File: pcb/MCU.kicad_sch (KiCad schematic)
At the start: 14 parts, among them U1 WeMos_S2_mini

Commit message: added connector and simulation link
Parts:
- removed TP28, TP29, TP30: TestPoint, Connector_PinHeader_1.00mm:PinHeader_1x01_P1.00mm_Vertical, symbol Connector:TestPoint
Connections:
- net SCR_QS_KS: now reaches U1.20 (GPIO6)
- net T_RPM: now reaches U1.19 (GPIO4)
- net T_CUT: now reaches U1.3 (GPIO5)
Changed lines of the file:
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@@
+		)
+	)
+	(global_label "SCR_QS_KS"
+		(shape input)
+		(at 86.36 64.77 0)
+		(fields_autoplaced yes)
+		(effects
+			(font
+				(size 1.27 1.27)
+			)
+			(justify left)
+		)
+		(property "Intersheetrefs" "${INTERSHEET_REFS}"
+			(at 100.0494 64.77 0)
+			(effects
+				(font
+					(size 1.27 1.27)
+				)
+				(justify left)
+				(hide yes)
+			)
 		)
 	)
@@
 		)
 	)
+	(global_label "T_RPM"
+		(shape input)
+		(at 86.36 59.69 0)
+		(fields_autoplaced yes)
+		(effects
+			(font
+				(size 1.27 1.27)
+			)
+			(justify left)
+		)
+		(property "Intersheetrefs" "${INTERSHEET_REFS}"
+			(at 95.2718 59.69 0)
+			(effects
+				(font
+					(size 1.27 1.27)
+				)
+				(justify left)
+				(hide yes)
+			)
+		)
+	)
+	(global_label "T_CUT"
+		(shape input)
+		(at 86.36 62.23 0)
+		(fields_autoplaced yes)
+		(effects
+			(font
+				(size 1.27 1.27)
+			)
+			(justify left)
+		)
+		(property "Intersheetrefs" "${INTERSHEET_REFS}"
+			(at 94.8485 62.23 0)
+			(effects
+				(font
+					(size 1.27 1.27)
+				)
+				(justify left)
+				(hide yes)
+			)
+		)
+	)
 	(global_label "PWM_VR"
 		(shape input)
@@
 	)
 	(symbol
-		(lib_id "Connector:TestPoint")
-		(at 86.36 64.77 270)
-		(unit 1)
-		(exclude_from_sim no)
-		(in_bom yes)
-		(on_board yes)
-		(dnp no)
-		(property "Reference" "TP28"
-			(at 91.186 64.77 90)
-			(effects
-				(font
-					(size 1.27 1.27)
-				)
-				(justify left)
-			)
-		)
-		(property "Value" "TestPoint"
-			(at 88.3921 67.31 0)
-			(effects
-				(font
-					(size 1.27 1.27)
-				)
-				(justify left)
-				(hide yes)
-			)
-		)
-		(property "Footprint" "Connector_PinHeader_1.00mm:PinHeader_1x01_P1.00mm_Vertical"
-			(at 86.36 69.85 0)
-			(effects
-				(font
-					(size 1.27 1.27)
-				)
-				(hide yes)
-			)
-		)
-		(property "Datasheet" "~"
-			(at 86.36 69.85 0)
-			(effects
-				(font
-					(size 1.27 1.27)
-				)
-				(hide yes)
-			)
-		)
-		(property "Description" "test point"
-			(at 86.36 64.77 0)
-			(effects
-				(font
-					(size 1.27 1.27)
-				)
-				(hide yes)
-			)
-		)
-		(pin "1"
-		)
-		(instances
-			(project "ecu-dev-board"
-				(path "/38d4df77-b5a0-4642-8410-8b13c21c2c3b/5baacb37-d82a-49c1-a6be-f8a839583d33"
-					(reference "TP28")
-					(unit 1)
-				)
-			)
-		)
-	)
-	(symbol
 		(lib_id "power:GND")
 		(at 265.43 52.07 0)
@@
 	)
 	(symbol
-		(lib_id "Connector:TestPoint")
-		(at 86.36 59.69 270)
-		(unit 1)
-		(exclude_from_sim no)
-		(in_bom yes)
-		(on_board yes)
-		(dnp no)
-		(property "Reference" "TP30"
-			(at 90.932 59.69 90)
-			(effects
-				(font
-					(size 1.27 1.27)
-				)
-				(justify left)
-			)
-		)
-		(property "Value" "TestPoint"
-			(at 88.3921 62.23 0)
-			(effects
-				(font
-					(size 1.27 1.27)
-				)
-				(justify left)
-				(hide yes)
-			)
-		)
-		(property "Footprint" "Connector_PinHeader_1.00mm:PinHeader_1x01_P1.00mm_Vertical"
-			(at 86.36 64.77 0)
-			(effects
-				(font
-					(size 1.27 1.27)
-				)
-				(hide yes)
-			)
-		)
-		(property "Datasheet" "~"
-			(at 86.36 64.77 0)
-			(effects
-				(font
-					(size 1.27 1.27)
-				)
-				(hide yes)
-			)
-		)
-		(property "Description" "test point"
-			(at 86.36 59.69 0)
-			(effects
-				(font
-					(size 1.27 1.27)
-				)
-				(hide yes)
-			)
-		)
-		(pin "1"
-		)
-		(instances
-			(project "ecu-dev-board"
-				(path "/38d4df77-b5a0-4642-8410-8b13c21c2c3b/5baacb37-d82a-49c1-a6be-f8a839583d33"
-					(reference "TP30")
-					(unit 1)
-				)
-			)
-		)
-	)
-	(symbol
 		(lib_id "power:GND")
 		(at 68.58 101.6 0)
@@
 					(unit 1)
 				)
-			)
-		)
-	)
-	(symbol
-		(lib_id "Connector:TestPoint")
-		(at 86.36 62.23 270)
-		(unit 1)
-		(exclude_from_sim no)
-		(in_bom yes)
-		(on_board yes)
-		(dnp no)
-		(property "Reference" "TP29"
-			(at 90.932 62.23 90)
-			(effects
-				(font
-					(size 1.27 1.27)
-				)
-				(justify left)
-			)
-		)
-		(property "Value" "TestPoint"
-			(at 88.3921 64.77 0)
-			(effects
-				(font
-					(size 1.27 1.27)
-				)
-				(justify left)
-				(hide yes)
-			)
-		)
-		(property "Footprint" "Connector_PinHeader_1.00mm:PinHeader_1x01_P1.00mm_Vertical"
-			(at 86.36 67.31 0)
-			(effects
-				(font
-					(size 1.27 1.27)
-				)
-				(hide yes)
-			)
-		)
-		(property "Datasheet" "~"
-			(at 86.36 67.31 0)
-			(effects
-				(font
-					(size 1.27 1.27)
-				)
-				(hide yes)
-			)
-		)
-		(property "Description" "test point"
-			(at 86.36 62.23 0)
-			(effects
-				(font
-					(size 1.27 1.27)
-				)
-				(hide yes)
-			)
-		)
-		(pin "1"
-		)
-		(instances
-			(project "ecu-dev-board"
-				(path "/38d4df77-b5a0-4642-8410-8b13c21c2c3b/5baacb37-d82a-49c1-a6be-f8a839583d33"
-					(reference "TP29")
-					(unit 1)
-				)

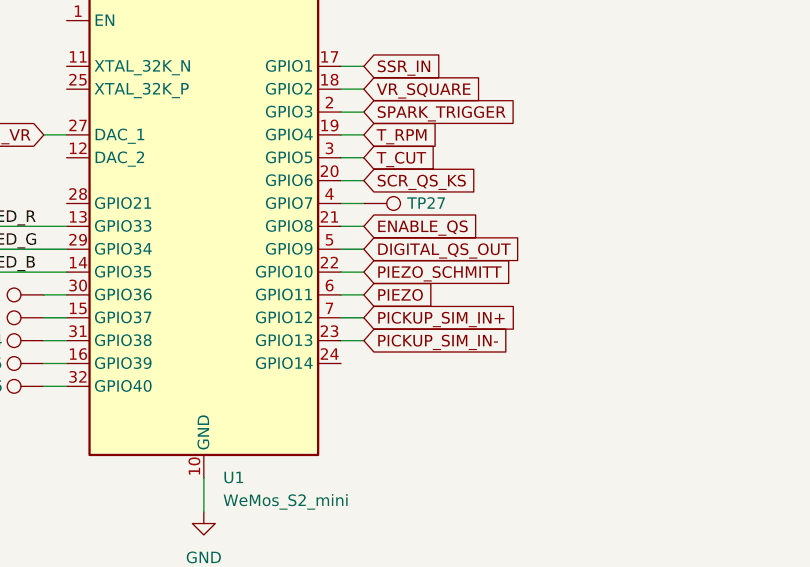
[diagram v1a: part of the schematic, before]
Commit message: added more connector tags
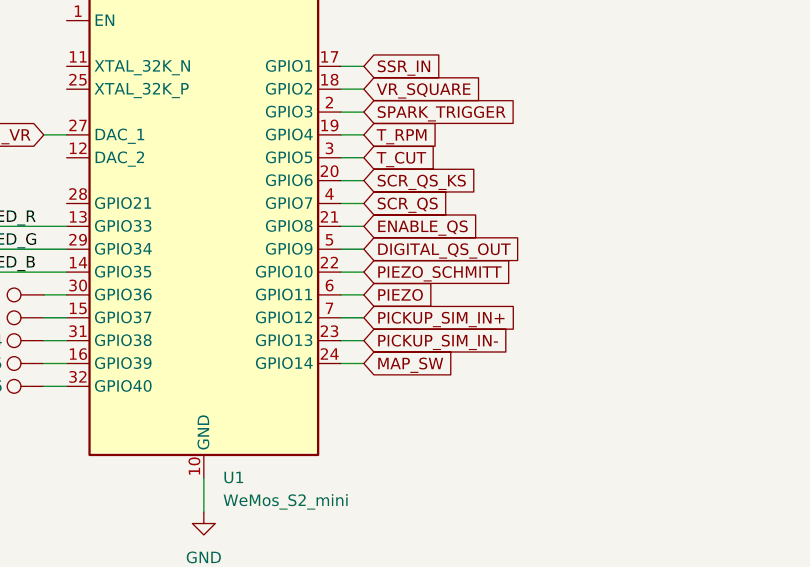
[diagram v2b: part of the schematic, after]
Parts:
- removed TP27: TestPoint, Connector_PinHeader_1.00mm:PinHeader_1x01_P1.00mm_Vertical, symbol Connector:TestPoint
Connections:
- net SCR_QS: now reaches U1.4 (GPIO7)
- net MAP_SW: now reaches U1.24 (GPIO14)
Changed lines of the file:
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@@
+	(wire
+		(pts
+			(xy 86.36 85.09) (xy 83.82 85.09)
+		)
+		(stroke
+			(width 0)
+			(type default)
+		)
+	)
 	(wire
 		(pts
@@
 		)
 	)
+	(global_label "MAP_SW"
+		(shape input)
+		(at 86.36 85.09 0)
+		(fields_autoplaced yes)
+		(effects
+			(font
+				(size 1.27 1.27)
+			)
+			(justify left)
+		)
+		(property "Intersheetrefs" "${INTERSHEET_REFS}"
+			(at 96.7837 85.09 0)
+			(effects
+				(font
+					(size 1.27 1.27)
+				)
+				(justify left)
+				(hide yes)
+			)
+		)
+	)
 	(global_label "SCR_QS_KS"
 		(shape input)
@@
 		(property "Intersheetrefs" "${INTERSHEET_REFS}"
 			(at 103.678 74.93 0)
+			(effects
+				(font
+					(size 1.27 1.27)
+				)
+				(justify left)
+				(hide yes)
+			)
+		)
+	)
+	(global_label "SCR_QS"
+		(shape input)
+		(at 86.36 67.31 0)
+		(fields_autoplaced yes)
+		(effects
+			(font
+				(size 1.27 1.27)
+			)
+			(justify left)
+		)
+		(property "Intersheetrefs" "${INTERSHEET_REFS}"
+			(at 96.6023 67.31 0)
 			(effects
 				(font
@@
 					(unit 1)
 				)
-			)
-		)
-	)
-	(symbol
-		(lib_id "Connector:TestPoint")
-		(at 86.36 67.31 270)
-		(unit 1)
-		(exclude_from_sim no)
-		(in_bom yes)
-		(on_board yes)
-		(dnp no)
-		(property "Reference" "TP27"
-			(at 91.186 67.31 90)
-			(effects
-				(font
-					(size 1.27 1.27)
-				)
-				(justify left)
-			)
-		)
-		(property "Value" "TestPoint"
-			(at 88.3921 69.85 0)
-			(effects
-				(font
-					(size 1.27 1.27)
-				)
-				(justify left)
-				(hide yes)
-			)
-		)
-		(property "Footprint" "Connector_PinHeader_1.00mm:PinHeader_1x01_P1.00mm_Vertical"
-			(at 86.36 72.39 0)
-			(effects
-				(font
-					(size 1.27 1.27)
-				)
-				(hide yes)
-			)
-		)
-		(property "Datasheet" "~"
-			(at 86.36 72.39 0)
-			(effects
-				(font
-					(size 1.27 1.27)
-				)
-				(hide yes)
-			)
-		)
-		(property "Description" "test point"
-			(at 86.36 67.31 0)
-			(effects
-				(font
-					(size 1.27 1.27)
-				)
-				(hide yes)
-			)
-		)
-		(pin "1"
-		)
-		(instances
-			(project "ecu-dev-board"
-				(path "/38d4df77-b5a0-4642-8410-8b13c21c2c3b/5baacb37-d82a-49c1-a6be-f8a839583d33"
-					(reference "TP27")
-					(unit 1)
-				)

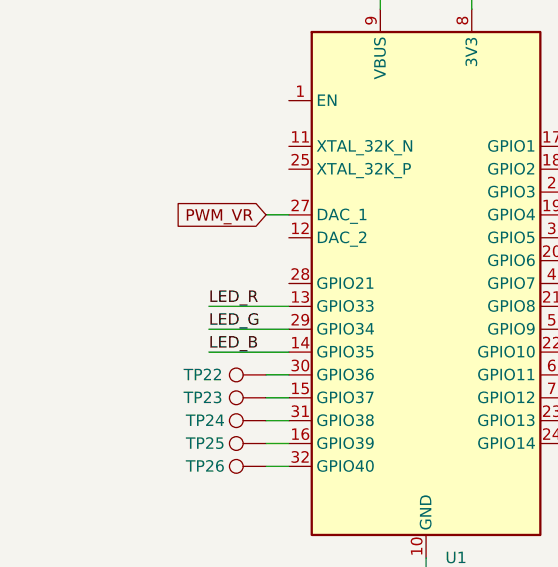
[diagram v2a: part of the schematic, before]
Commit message: enhanced pickup simulation
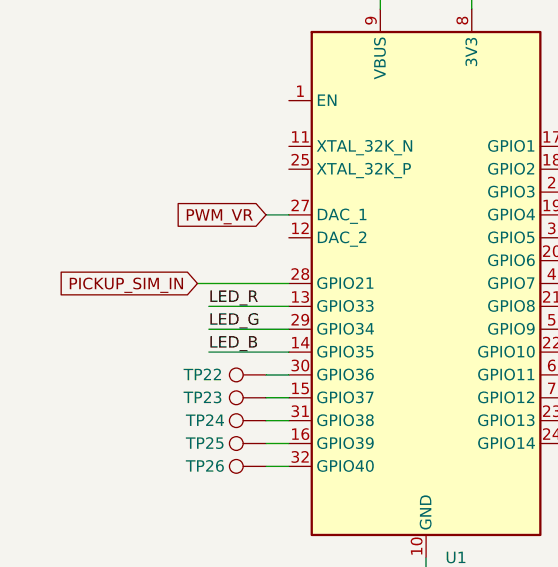
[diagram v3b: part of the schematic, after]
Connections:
- net PICKUP_SIM_IN: now reaches U1.28 (GPIO21)
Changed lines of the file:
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@@
+	(wire
+		(pts
+			(xy 43.18 67.31) (xy 53.34 67.31)
+		)
+		(stroke
+			(width 0)
+			(type default)
+		)
+	)
 	(wire
 		(pts
@@
 				(hide yes)
 			)
+		)
+	)
+	(global_label "PICKUP_SIM_IN"
+		(shape input)
+		(at 43.18 67.31 180)
+		(fields_autoplaced yes)
+		(effects
+			(font
+				(size 1.27 1.27)
+			)
+			(justify right)
+		)
+		(property "Intersheetrefs" "${INTERSHEET_REFS}"
+			(at 26.0433 67.31 0)
+			(effects
+				(font
+					(size 1.27 1.27)
+				)
+				(justify right)
+				(hide yes)
+			)

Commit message: changed capacitors and resistors footprints from 0201 to 0603
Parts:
- R50, R51, R52: footprint Resistor_SMD:R_0201_0603Metric -> Resistor_SMD:R_0603_1608Metric
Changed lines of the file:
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@@
 			)
 		)
-		(property "Footprint" "Resistor_SMD:R_0201_0603Metric"
+		(property "Footprint" "Resistor_SMD:R_0603_1608Metric"
 			(at 236.22 44.958 90)
 			(effects
@@
 			)
 		)
-		(property "Footprint" "Resistor_SMD:R_0201_0603Metric"
+		(property "Footprint" "Resistor_SMD:R_0603_1608Metric"
 			(at 236.22 50.038 90)
 			(effects
@@
 			)
 		)
-		(property "Footprint" "Resistor_SMD:R_0201_0603Metric"
+		(property "Footprint" "Resistor_SMD:R_0603_1608Metric"
 			(at 236.22 55.118 90)
 			(effects

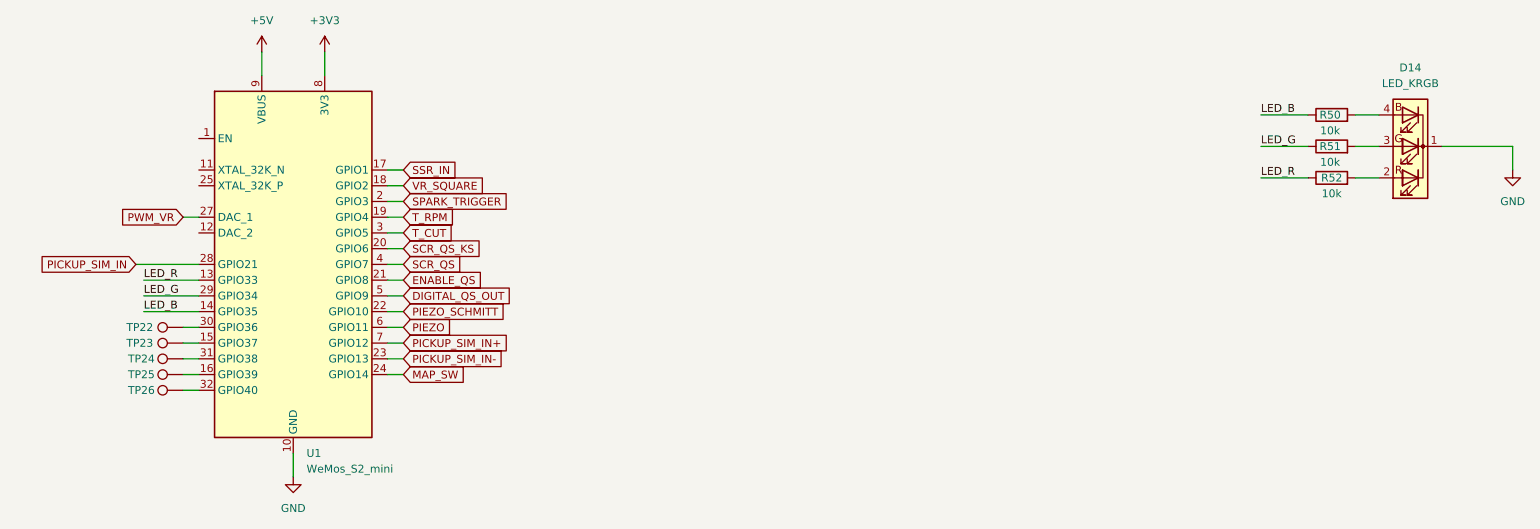
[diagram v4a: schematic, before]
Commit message: changed SCR drives to pnp drive and started schematic revision
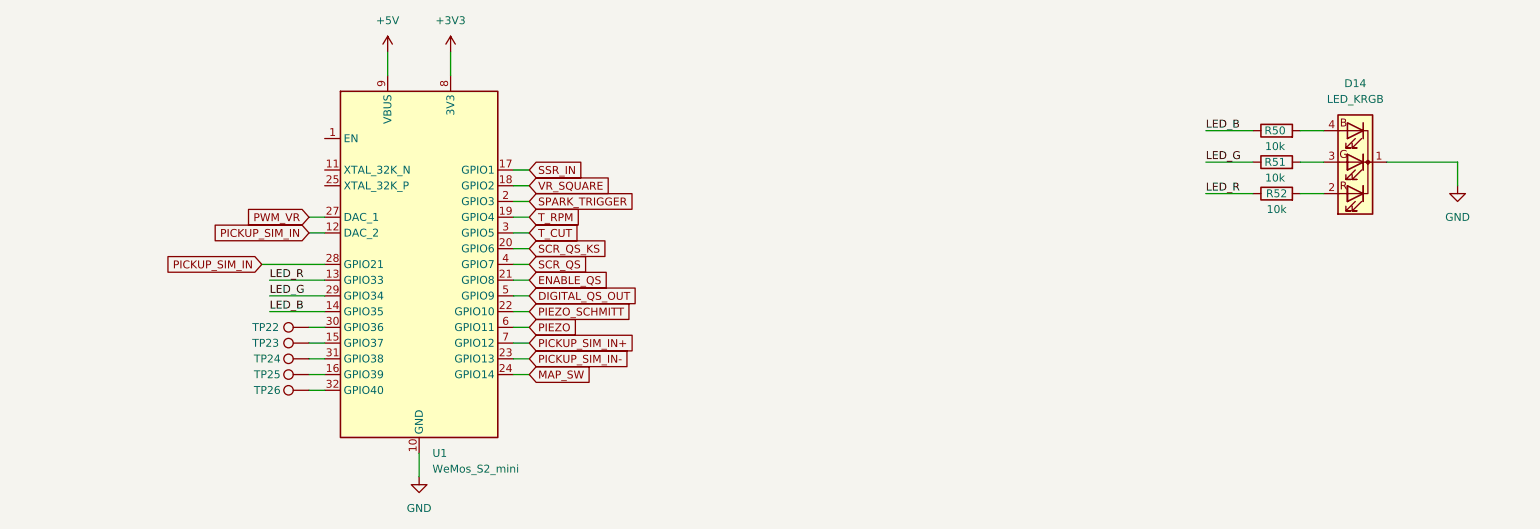
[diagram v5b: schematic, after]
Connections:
- net PICKUP_SIM_IN: now also U1.12 (DAC_2)
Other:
- moved on the sheet: D14, R50, R51, R52, TP22, TP23, TP24, TP25, U1

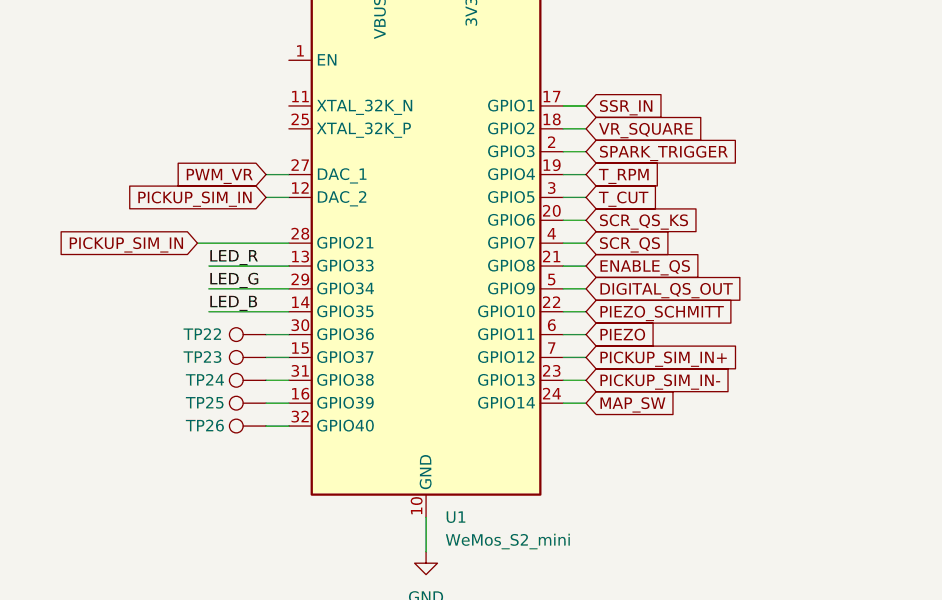
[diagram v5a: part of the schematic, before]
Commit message: simplified pickup simulation pinout
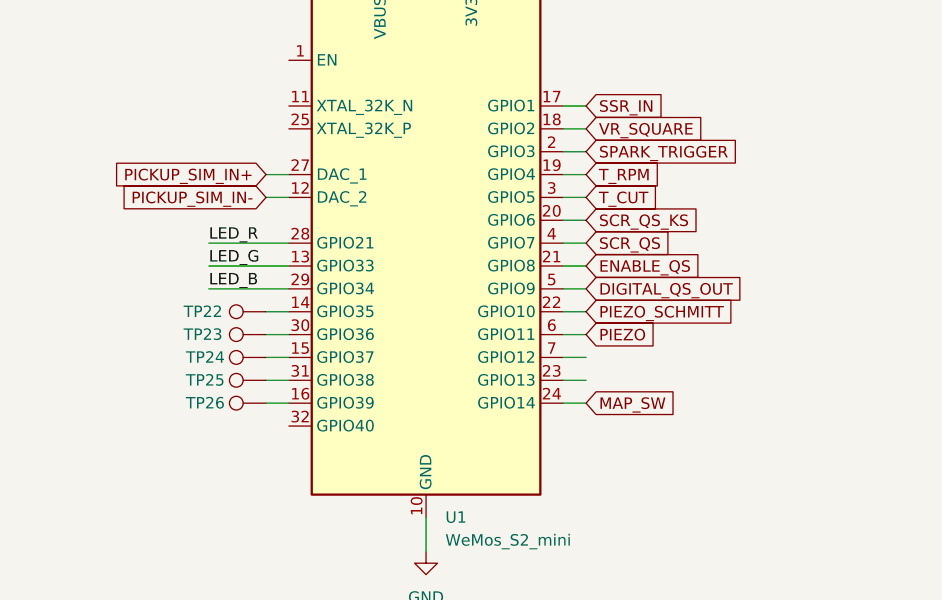
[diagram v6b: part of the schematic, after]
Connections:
- net PWM_VR is gone; now on net PICKUP_SIM_IN+: U1.27 (DAC_1)
- net LED_B: now also U1.29 (GPIO34); no longer U1.14 (GPIO35)
- net LED_G: now also U1.13 (GPIO33); no longer U1.29 (GPIO34)
- net LED_R: now also U1.28 (GPIO21); no longer U1.13 (GPIO33)
- net PICKUP_SIM_IN+: no longer U1.7 (GPIO12)
- net PICKUP_SIM_IN-: now also U1.12 (DAC_2); no longer U1.23 (GPIO13)
- net at TP23.1: now also U1.30 (GPIO36); no longer U1.15 (GPIO37)
- net at TP22.1: now also U1.14 (GPIO35); no longer U1.30 (GPIO36)
- net at U1.16 (GPIO39): now also TP26.1; no longer TP25.1
- net at TP24.1: now also U1.15 (GPIO37); no longer U1.31 (GPIO38)
- net at U1.32 (GPIO40): no longer TP26.1
- removed net PICKUP_SIM_IN: U1.12 (DAC_2), U1.28 (GPIO21)
- new net: TP25.1, U1.31 (GPIO38)
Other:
- moved on the sheet: TP22, TP23, TP24, TP25, TP26

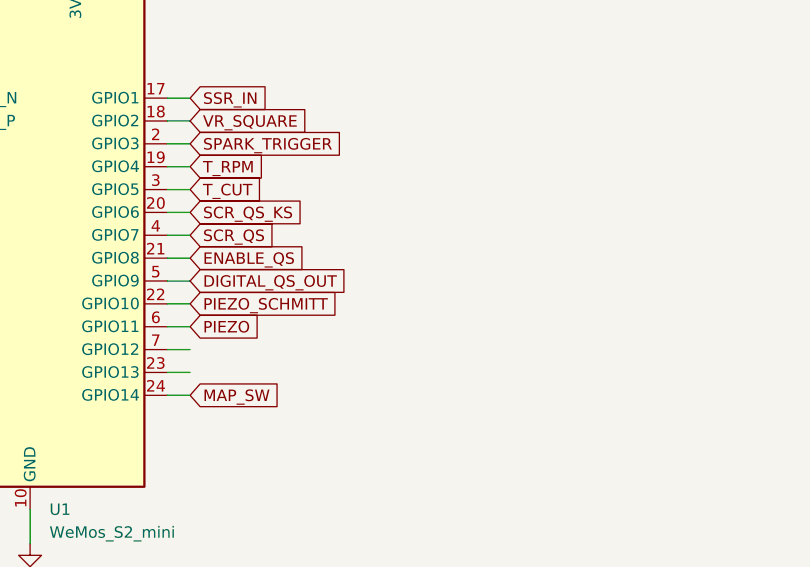
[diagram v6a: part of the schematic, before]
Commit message: added proper handling and comments to QS digital sensor
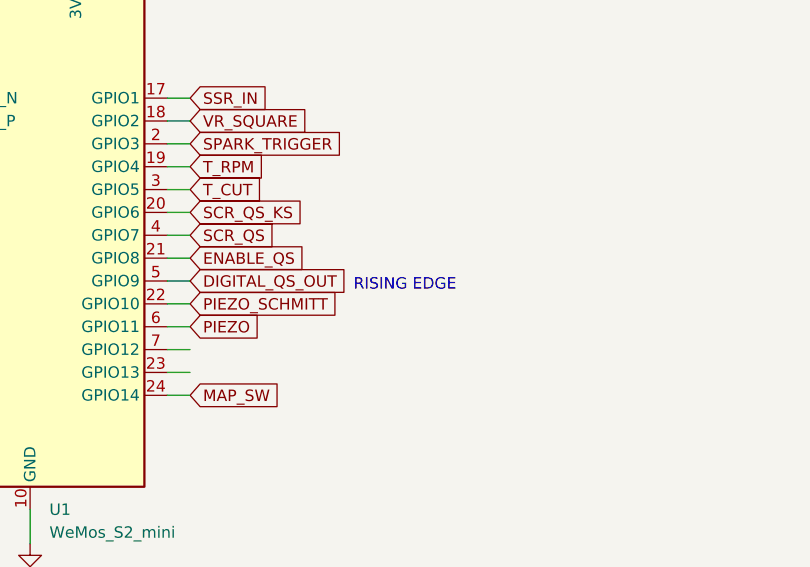
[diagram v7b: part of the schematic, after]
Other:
- note added: "RISING EDGE"
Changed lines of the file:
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@@
 	(generator_version "9.0")
 	(paper "A4")
+	(text "RISING EDGE"
+		(exclude_from_sim no)
+		(at 130.556 72.898 0)
+		(effects
+			(font
+				(size 1.27 1.27)
+			)
+		)
+	)
 	(wire
 		(pts
